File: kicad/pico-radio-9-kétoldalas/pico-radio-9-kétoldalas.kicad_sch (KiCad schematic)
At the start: 53 parts, among them J1 FM antenna, J2 SW antenna, J3 MW/SW antenna kapcsoló, J4 HF Amplifier, J5 Batterry, J6 KY-040 Rotary, Q1 PN2222A, Q2 PN2222A, Q3 PN2222A, SW1 Reset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

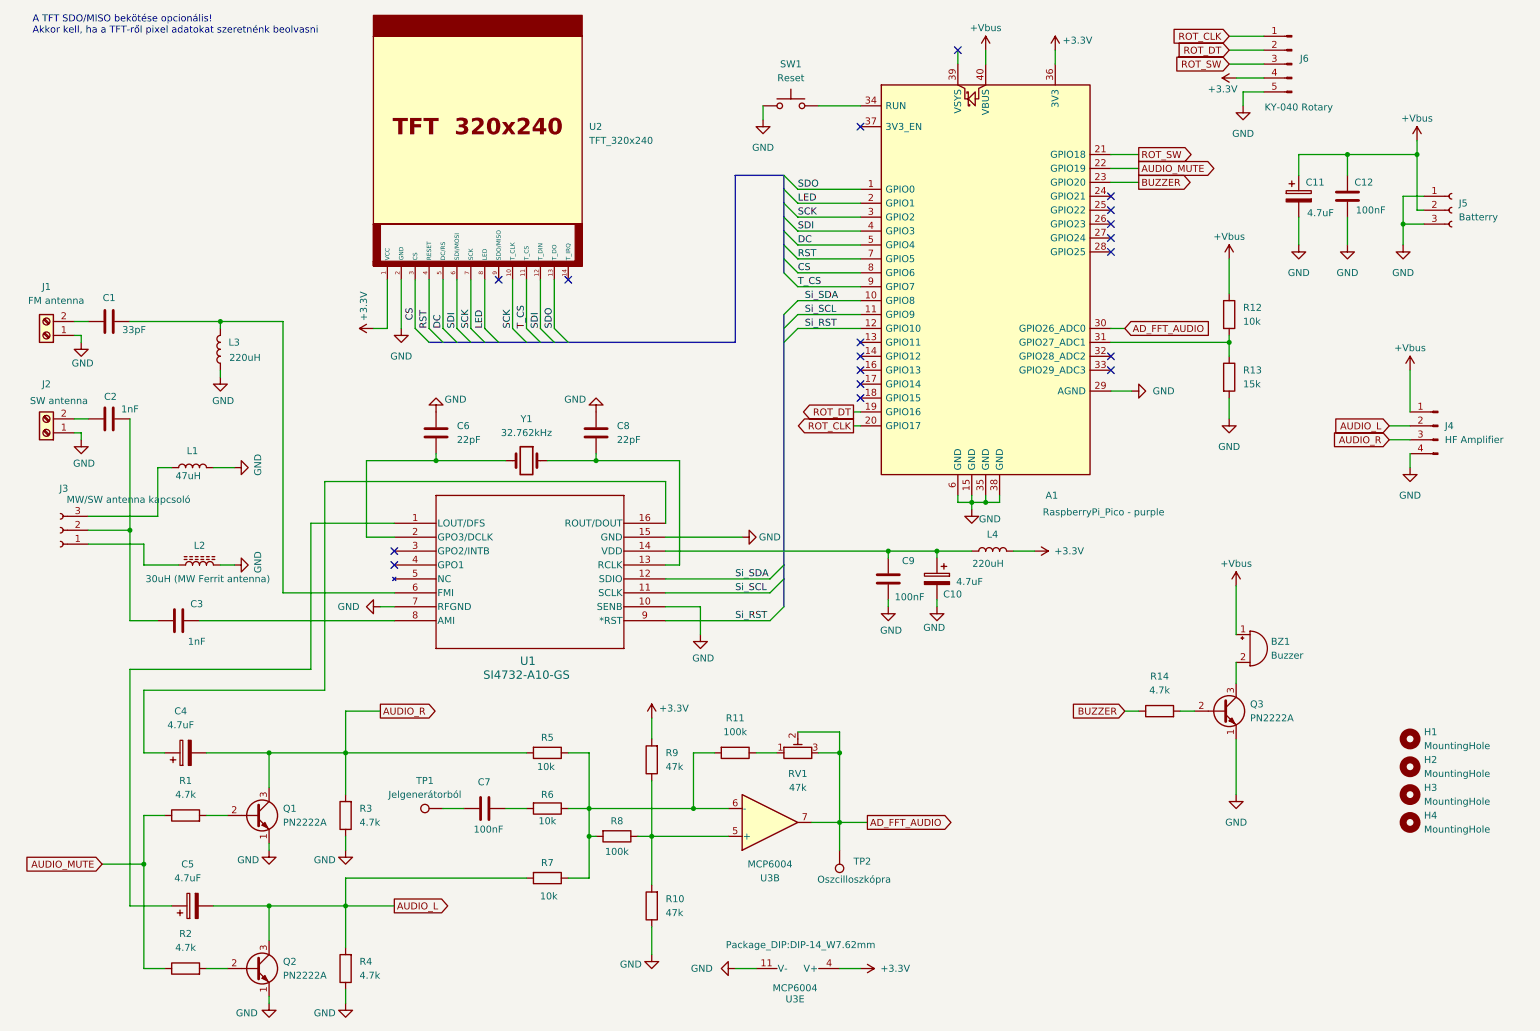
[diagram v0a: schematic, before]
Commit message: Vsys - Vbus power modification
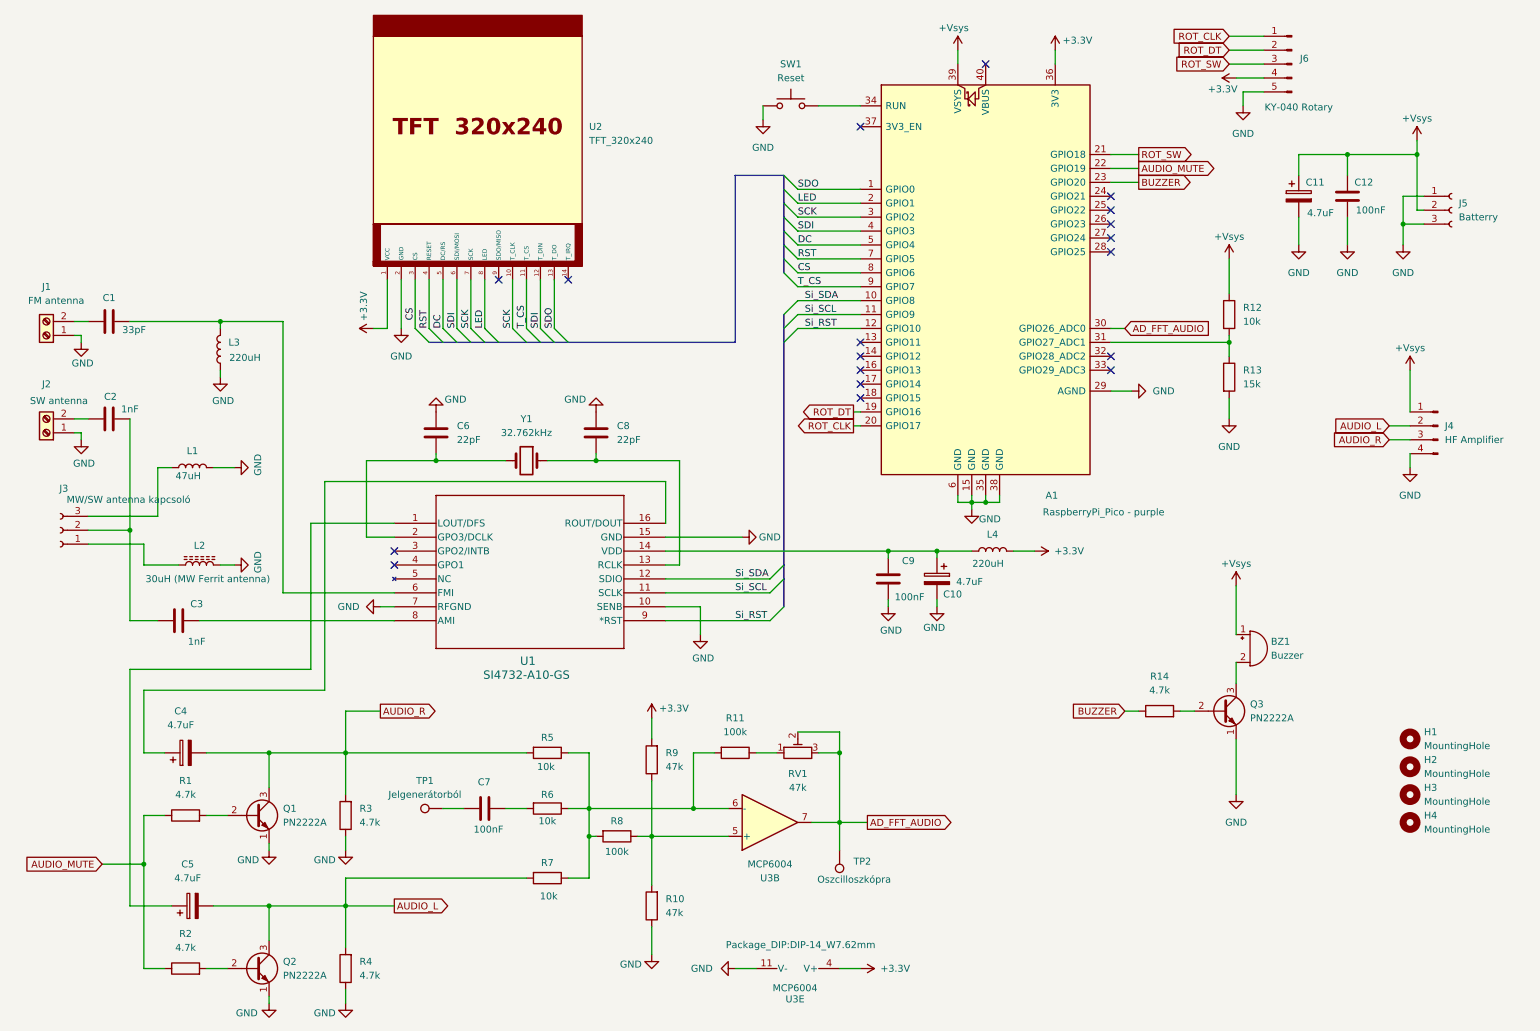
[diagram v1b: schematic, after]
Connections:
- net +Vsys: now reaches A1.39 (VSYS)
- net +Vsys: now also BZ1.1 (+), C11.1, C12.1, J4.1 (Pin_1), J5.2 (Pin_2), R12.1
- removed net +Vbus: A1.40 (VBUS), BZ1.1 (+), C11.1, C12.1, J4.1 (Pin_1), J5.2 (Pin_2), R12.1
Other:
- note removed: "A TFT SDO/MISO bekötése opcionális! Akkor kell, ha a TFT-ről pixel adatokat szeretnénk beolvasni"
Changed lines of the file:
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@@
 		(date "2025-08-04")
 	)
-	(text "A TFT SDO/MISO bekötése opcionális!\nAkkor kell, ha a TFT-ről pixel adatokat szeretnénk beolvasni"
-		(exclude_from_sim no)
-		(at 13.97 15.748 0)
-		(effects
-			(font
-				(size 1.27 1.27)
-			)
-			(justify left)
-		)
-	)
 	(junction
 		(at 179.07 111.76)
@@
 	)
 	(no_connect
-		(at 182.88 20.32)
-	)
-	(no_connect
 		(at 210.82 76.2)
 	)
@@
 	)
 	(no_connect
+		(at 187.96 22.86)
+	)
+	(no_connect
 		(at 210.82 57.15)
 	)
@@
 	(wire
 		(pts
-			(xy 187.96 20.32) (xy 187.96 22.86)
-		)
-		(stroke
-			(width 0)
-			(type default)
-		)
-	)
-	(wire
-		(pts
 			(xy 74.93 95.25) (xy 87.63 95.25)
 		)
@@
 			)
 		)
-		(property "Value" "+Vbus"
+		(property "Value" "+Vsys"
 			(at 265.43 74.676 0)
 			(effects
@@
 			)
 		)
-		(property "Value" "+Vbus"
+		(property "Value" "+Vsys"
 			(at 232.41 54.356 0)
 			(effects
@@
 	)
 	(symbol
-		(lib_id "Device:R")
-		(at 107.95 148.59 270)
+		(lib_id "power:+BATT")
+		(at 182.88 20.32 0)
 		(unit 1)
 		(exclude_from_sim no)
@@
 		(on_board yes)
 		(dnp no)
-		(property "Reference" "R5"
-			(at 107.95 145.796 90)
+		(property "Reference" "#PWR022"
+			(at 182.88 24.13 0)
 			(effects
 				(font
 					(size 1.27 1.27)
 				)
+				(hide yes)
 			)
 		)
-		(property "Value" "10k"
-			(at 107.696 151.13 90)
+		(property "Value" "+Vsys"
+			(at 182.118 16.256 0)
 			(effects
 				(font
@@
 			)
 		)
-		(property "Footprint" "Resistor_THT:R_Axial_DIN0207_L6.3mm_D2.5mm_P10.16mm_Horizontal"
-			(at 107.95 146.812 90)
+		(property "Footprint" ""
+			(at 182.88 20.32 0)
 			(effects
 				(font
@@
 			)
 		)
-		(property "Datasheet" "~"
-			(at 107.95 148.59 0)
+		(property "Datasheet" ""
+			(at 182.88 20.32 0)
 			(effects
 				(font
@@
 			)
 		)
-		(property "Description" "Resistor"
-			(at 107.95 148.59 0)
+		(property "Description" "Power symbol creates a global label with name \"+BATT\""
+			(at 182.88 20.32 0)
 			(effects
 				(font
@@
 		(pin "1"
 		)
-		(pin "2"
-		)
 		(instances
-			(project "pico-radio-9"
+			(project "pico-radio-9-kétoldalas"
 				(path "/b9640508-dcc6-4f6b-830f-c53a732dcb5b"
-					(reference "R5")
+					(reference "#PWR022")
 					(unit 1)
 				)
@@
 	)
 	(symbol
-		(lib_id "power:+BATT")
-		(at 187.96 20.32 0)
+		(lib_id "Device:R")
+		(at 107.95 148.59 270)
 		(unit 1)
 		(exclude_from_sim no)
@@
 		(on_board yes)
 		(dnp no)
-		(property "Reference" "#PWR025"
-			(at 187.96 24.13 0)
+		(property "Reference" "R5"
+			(at 107.95 145.796 90)
 			(effects
 				(font
 					(size 1.27 1.27)
 				)
-				(hide yes)
 			)
 		)
-		(property "Value" "+Vbus"
-			(at 187.96 16.256 0)
+		(property "Value" "10k"
+			(at 107.696 151.13 90)
 			(effects
 				(font
@@
 			)
 		)
-		(property "Footprint" ""
-			(at 187.96 20.32 0)
+		(property "Footprint" "Resistor_THT:R_Axial_DIN0207_L6.3mm_D2.5mm_P10.16mm_Horizontal"
+			(at 107.95 146.812 90)
 			(effects
 				(font
@@
 			)
 		)
-		(property "Datasheet" ""
-			(at 187.96 20.32 0)
+		(property "Datasheet" "~"
+			(at 107.95 148.59 0)
 			(effects
 				(font
@@
 			)
 		)
-		(property "Description" "Power symbol creates a global label with name \"+BATT\""
-			(at 187.96 20.32 0)
+		(property "Description" "Resistor"
+			(at 107.95 148.59 0)
 			(effects
 				(font
@@
 		(pin "1"
 		)
+		(pin "2"
+		)
 		(instances
-			(project ""
+			(project "pico-radio-9"
 				(path "/b9640508-dcc6-4f6b-830f-c53a732dcb5b"
-					(reference "#PWR025")
+					(reference "R5")
 					(unit 1)
 				)
@@
 			)
 		)
-		(property "Value" "+Vbus"
+		(property "Value" "+Vsys"
 			(at 266.7 32.766 0)
 			(effects
@@
 			)
 		)
-		(property "Value" "+Vbus"
+		(property "Value" "+Vsys"
 			(at 233.68 114.046 0)
 			(effects

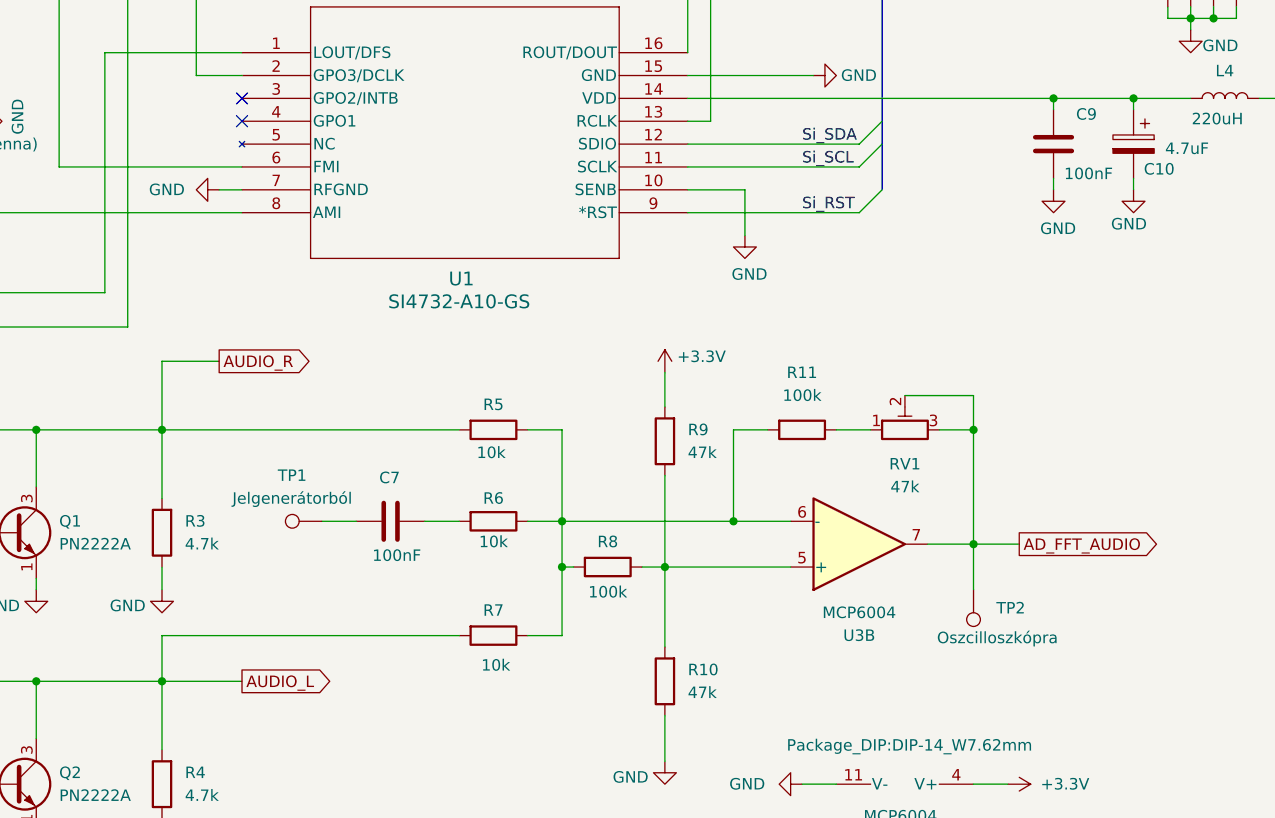
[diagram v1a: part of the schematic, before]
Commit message: Add capacitors C13 and C14 to the schematic and update connections
- Added capacitor C13 (100nF) at coordinates (96.52, 148.59) with appropriate properties.
- Added capacitor C14 (100nF) at coordinates (96.52, 171.45) with appropriate properties.
- Updated wire connections for C13 and C14.
- Changed the value of resistor R1 from 100k to 47k.
- Adjusted the position of capacitor C7 for better layout.
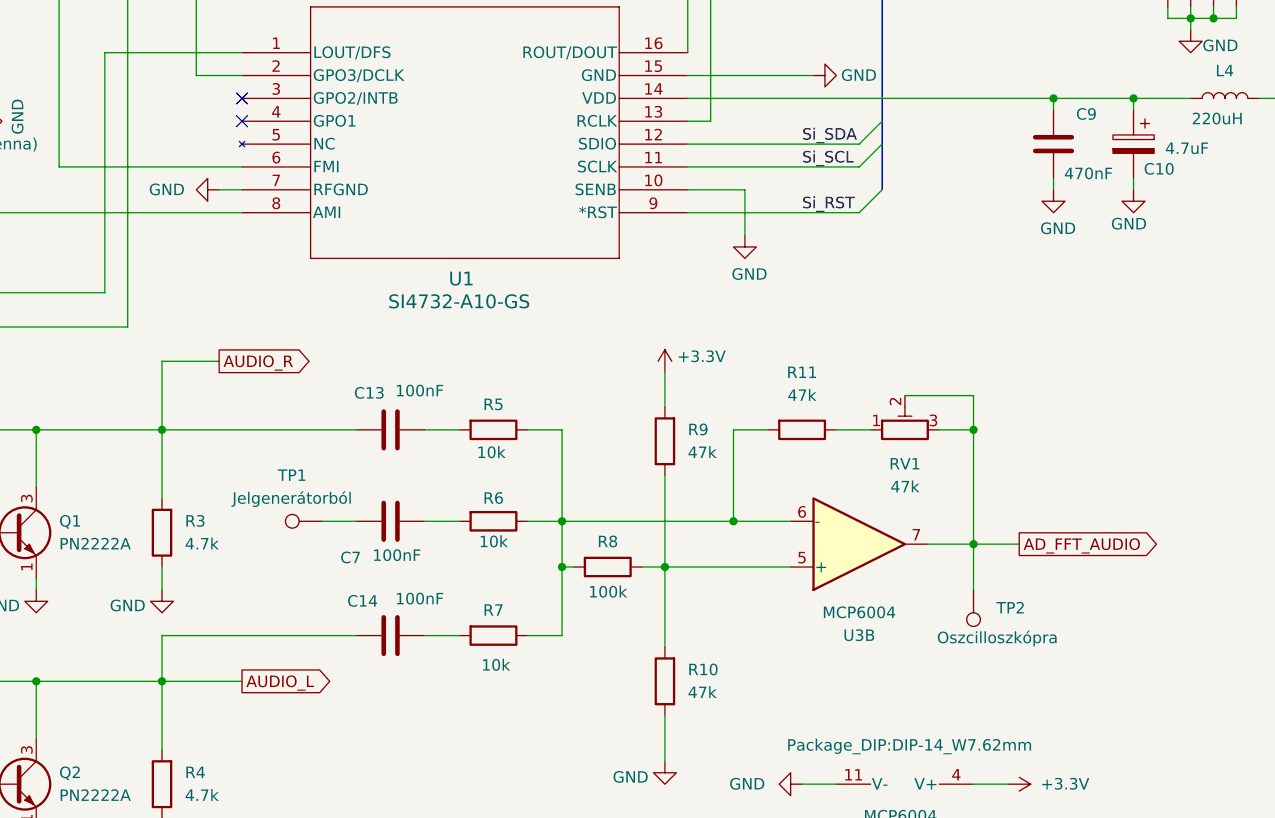
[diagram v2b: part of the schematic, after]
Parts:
- added C13, C14: 100nF, Capacitor_THT:C_Disc_D5.0mm_W2.5mm_P2.50mm, symbol Device:C
- C9: value 100nF -> 470nF
- R11: value 100k -> 47k
- R5, R7: footprint Resistor_THT:R_Axial_DIN0207_L6.3mm_D2.5mm_P10.16mm_Horizontal -> Resistor_THT:R_Axial_DIN0207_L6.3mm_D2.5mm_P2.54mm_Vertical
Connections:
- net AUDIO_L: now also C14.2; no longer R7.2
- net AUDIO_R: now also C13.2; no longer R5.2
- new net: C14.1, R7.2
- new net: C13.1, R5.2
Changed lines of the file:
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@@
 	(title_block
 		(title "Pico radio-9 (kétoldalas panel)")
-		(date "2025-08-04")
+		(date "2026-01-28")
 	)
 	(junction
@@
 	(wire
 		(pts
+			(xy 71.12 148.59) (xy 92.71 148.59)
+		)
+		(stroke
+			(width 0)
+			(type default)
+		)
+	)
+	(wire
+		(pts
 			(xy 71.12 148.59) (xy 57.15 148.59)
 		)
@@
 		)
 	)
-	(wire
-		(pts
-			(xy 71.12 148.59) (xy 104.14 148.59)
-		)
-		(stroke
-			(width 0)
-			(type default)
-		)
-	)
 	(bus
 		(pts
@@
 	(wire
 		(pts
+			(xy 100.33 148.59) (xy 104.14 148.59)
+		)
+		(stroke
+			(width 0)
+			(type default)
+		)
+	)
+	(wire
+		(pts
 			(xy 153.67 71.12) (xy 165.1 71.12)
 		)
@@
 	(wire
 		(pts
+			(xy 100.33 171.45) (xy 104.14 171.45)
+		)
+		(stroke
+			(width 0)
+			(type default)
+		)
+	)
+	(wire
+		(pts
 			(xy 86.36 62.23) (xy 86.36 71.12)
 		)
@@
 		)
 	)
+	(wire
+		(pts
+			(xy 71.12 171.45) (xy 92.71 171.45)
+		)
+		(stroke
+			(width 0)
+			(type default)
+		)
+	)
 	(bus
 		(pts
@@
 	(wire
 		(pts
-			(xy 71.12 171.45) (xy 104.14 171.45)
-		)
-		(stroke
-			(width 0)
-			(type default)
-		)
-	)
-	(wire
-		(pts
 			(xy 93.98 62.23) (xy 93.98 71.12)
 		)
@@
 			)
 		)
-		(property "Value" "100k"
+		(property "Value" "47k"
 			(at 142.24 144.78 90)
 			(effects
@@
 	)
 	(symbol
+		(lib_id "Device:C")
+		(at 96.52 171.45 270)
+		(unit 1)
+		(exclude_from_sim no)
+		(in_bom yes)
+		(on_board yes)
+		(dnp no)
+		(property "Reference" "C14"
+			(at 91.694 167.64 90)
+			(effects
+				(font
+					(size 1.27 1.27)
+				)
+				(justify left)
+			)
+		)
+		(property "Value" "100nF"
+			(at 97.028 167.386 90)
+			(effects
+				(font
+					(size 1.27 1.27)
+				)
+				(justify left)
+			)
+		)
+		(property "Footprint" "Capacitor_THT:C_Disc_D5.0mm_W2.5mm_P2.50mm"
+			(at 92.71 172.4152 0)
+			(effects
+				(font
+					(size 1.27 1.27)
+				)
+				(hide yes)
+			)
+		)
+		(property "Datasheet" "~"
+			(at 96.52 171.45 0)
+			(effects
+				(font
+					(size 1.27 1.27)
+				)
+				(hide yes)
+			)
+		)
+		(property "Description" "Unpolarized capacitor"
+			(at 96.52 171.45 0)
+			(effects
+				(font
+					(size 1.27 1.27)
+				)
+				(hide yes)
+			)
+		)
+		(pin "1"
+		)
+		(pin "2"
+		)
+		(instances
+			(project "pico-radio-9-kétoldalas"
+				(path "/b9640508-dcc6-4f6b-830f-c53a732dcb5b"
+					(reference "C14")
+					(unit 1)
+				)
+			)
+		)
+	)
+	(symbol
 		(lib_id "Device:R")
 		(at 127 176.53 180)
@@
 	)
 	(symbol
+		(lib_id "Device:C")
+		(at 96.52 148.59 270)
+		(unit 1)
+		(exclude_from_sim no)
+		(in_bom yes)
+		(on_board yes)
+		(dnp no)
+		(property "Reference" "C13"
+			(at 92.456 144.526 90)
+			(effects
+				(font
+					(size 1.27 1.27)
+				)
+				(justify left)
+			)
+		)
+		(property "Value" "100nF"
+			(at 97.028 144.272 90)
+			(effects
+				(font
+					(size 1.27 1.27)
+				)
+				(justify left)
+			)
+		)
+		(property "Footprint" "Capacitor_THT:C_Disc_D5.0mm_W2.5mm_P2.50mm"
+			(at 92.71 149.5552 0)
+			(effects
+				(font
+					(size 1.27 1.27)
+				)
+				(hide yes)
+			)
+		)
+		(property "Datasheet" "~"
+			(at 96.52 148.59 0)
+			(effects
+				(font
+					(size 1.27 1.27)
+				)
+				(hide yes)
+			)
+		)
+		(property "Description" "Unpolarized capacitor"
+			(at 96.52 148.59 0)
+			(effects
+				(font
+					(size 1.27 1.27)
+				)
+				(hide yes)
+			)
+		)
+		(pin "1"
+		)
+		(pin "2"
+		)
+		(instances
+			(project "pico-radio-9-kétoldalas"
+				(path "/b9640508-dcc6-4f6b-830f-c53a732dcb5b"
+					(reference "C13")
+					(unit 1)
+				)
+			)
+		)
+	)
+	(symbol
 		(lib_id "Transistor_BJT:PN2222A")
 		(at 54.61 187.96 0)
@@
 		(dnp no)
 		(property "Reference" "C7"
-			(at 95.25 153.924 90)
+			(at 90.932 162.814 90)
 			(effects
 				(font
@@
 			)
 		)
-		(property "Footprint" "Resistor_THT:R_Axial_DIN0207_L6.3mm_D2.5mm_P10.16mm_Horizontal"
+		(property "Footprint" "Resistor_THT:R_Axial_DIN0207_L6.3mm_D2.5mm_P2.54mm_Vertical"
 			(at 107.95 169.672 90)
 			(effects
@@
 			)
 		)
-		(property "Footprint" "Resistor_THT:R_Axial_DIN0207_L6.3mm_D2.5mm_P10.16mm_Horizontal"
+		(property "Footprint" "Resistor_THT:R_Axial_DIN0207_L6.3mm_D2.5mm_P2.54mm_Vertical"
 			(at 107.95 146.812 90)
 			(effects
@@
 			)
 		)
-		(property "Value" "100nF"
+		(property "Value" "470nF"
 			(at 176.784 120.142 0)
 			(effects
